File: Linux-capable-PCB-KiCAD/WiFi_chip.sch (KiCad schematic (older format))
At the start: 2 parts

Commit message: Added some documents
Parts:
- added C? (x4): 100n, symbol device:C
- added C?: 5.6p, symbol device:C
- added L?: NC, symbol device:L
- added Y?: 26 MHz, symbol device:Crystal_GND23
- R?: symbol Device:R -> Linux-capable-PCB-KiCAD-rescue:R-Device
- U?: symbol ESP8089:ESP8089 -> Linux-capable-PCB-KiCAD-rescue:ESP8089-ESP8089
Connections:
- net labels added: SD_CLK, SD_CMD, SD_D0, SD_D1, SD_D2, SD_D3, VDD33, VDIO, WIFI_ANT, WIFI_EN
- wire segments 7 -> 59

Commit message: RAM cip je spojen
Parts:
- C? (x5): symbol device:C -> Linux-capable-PCB-KiCAD-rescue:C-device
- L?: symbol device:L -> Linux-capable-PCB-KiCAD-rescue:L-device
- Y?: symbol device:Crystal_GND23 -> Linux-capable-PCB-KiCAD-rescue:Crystal_GND23-device
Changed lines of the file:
@@
 $Descr A4 11693 8268
 encoding utf-8
-Sheet 3 3
+Sheet 3 4
 Title ""
 Date ""
@@
 Connection ~ 6600 4200
 $Comp
-L device:C C?
+L Linux-capable-PCB-KiCAD-rescue:C-device C?
 U 1 1 62B23B89
 P 6900 4450
@@
 	4550 3600 3300 3600
 $Comp
-L device:C C?
+L Linux-capable-PCB-KiCAD-rescue:C-device C?
 U 1 1 62B24ACF
 P 3000 3600
@@
 $EndComp
 $Comp
-L device:L L?
+L Linux-capable-PCB-KiCAD-rescue:L-device L?
 U 1 1 62B2523E
 P 3300 3900
@@
 Connection ~ 5350 1900
 $Comp
-L device:C C?
+L Linux-capable-PCB-KiCAD-rescue:C-device C?
 U 1 1 62B27ADB
 P 3800 2150
@@
 Connection ~ 3800 1900
 $Comp
-L device:Crystal_GND23 Y?
+L Linux-capable-PCB-KiCAD-rescue:Crystal_GND23-device Y?
 U 1 1 62B29AE8
 P 6050 1900
@@
 	6050 2100 6050 2150
 $Comp
-L device:C C?
+L Linux-capable-PCB-KiCAD-rescue:C-device C?
 U 1 1 62B2DA78
 P 5550 1450
@@
 $EndComp
 $Comp
-L device:C C?
+L Linux-capable-PCB-KiCAD-rescue:C-device C?
 U 1 1 62B2DE8D
 P 6800 1450

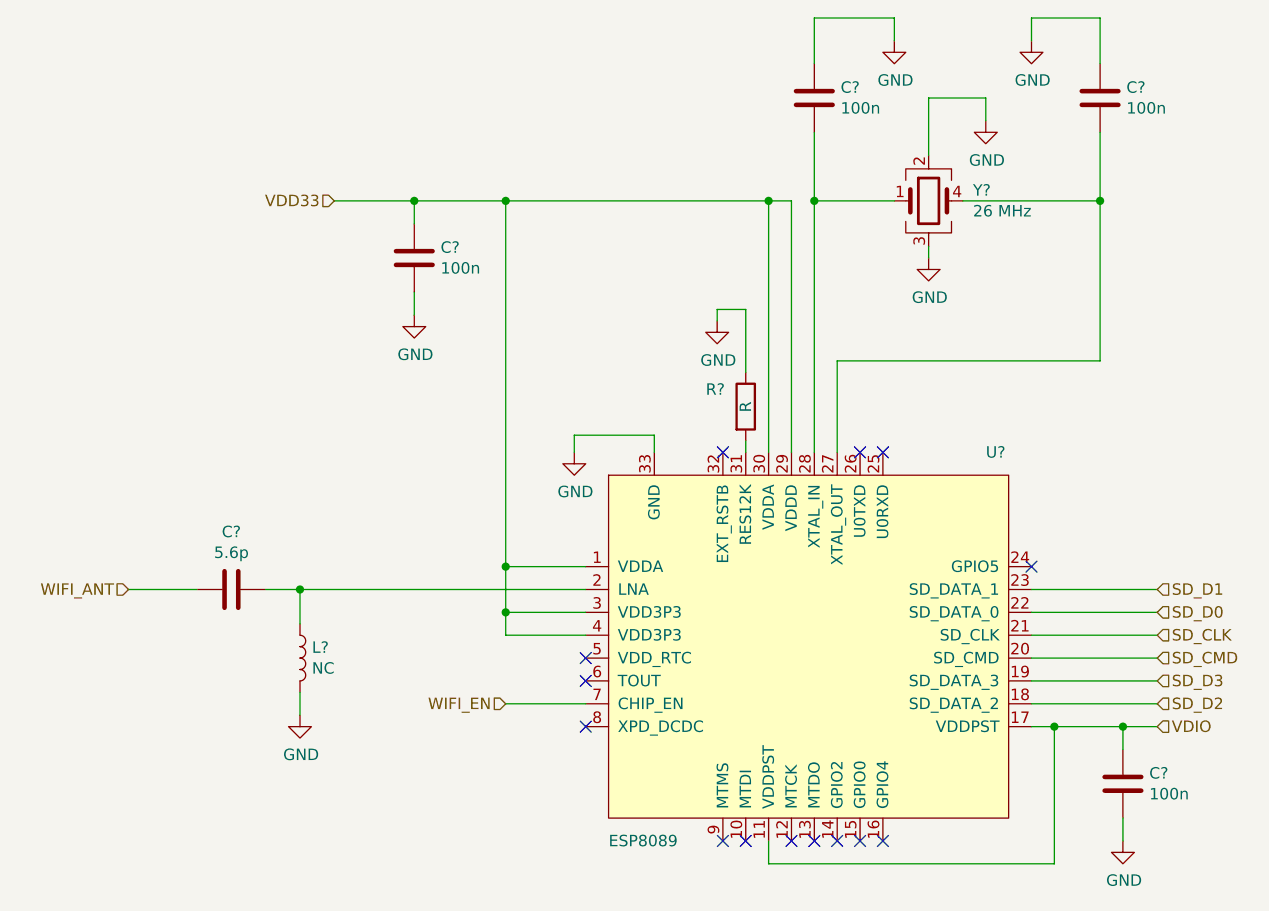
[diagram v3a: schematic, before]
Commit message: Power supply schematics
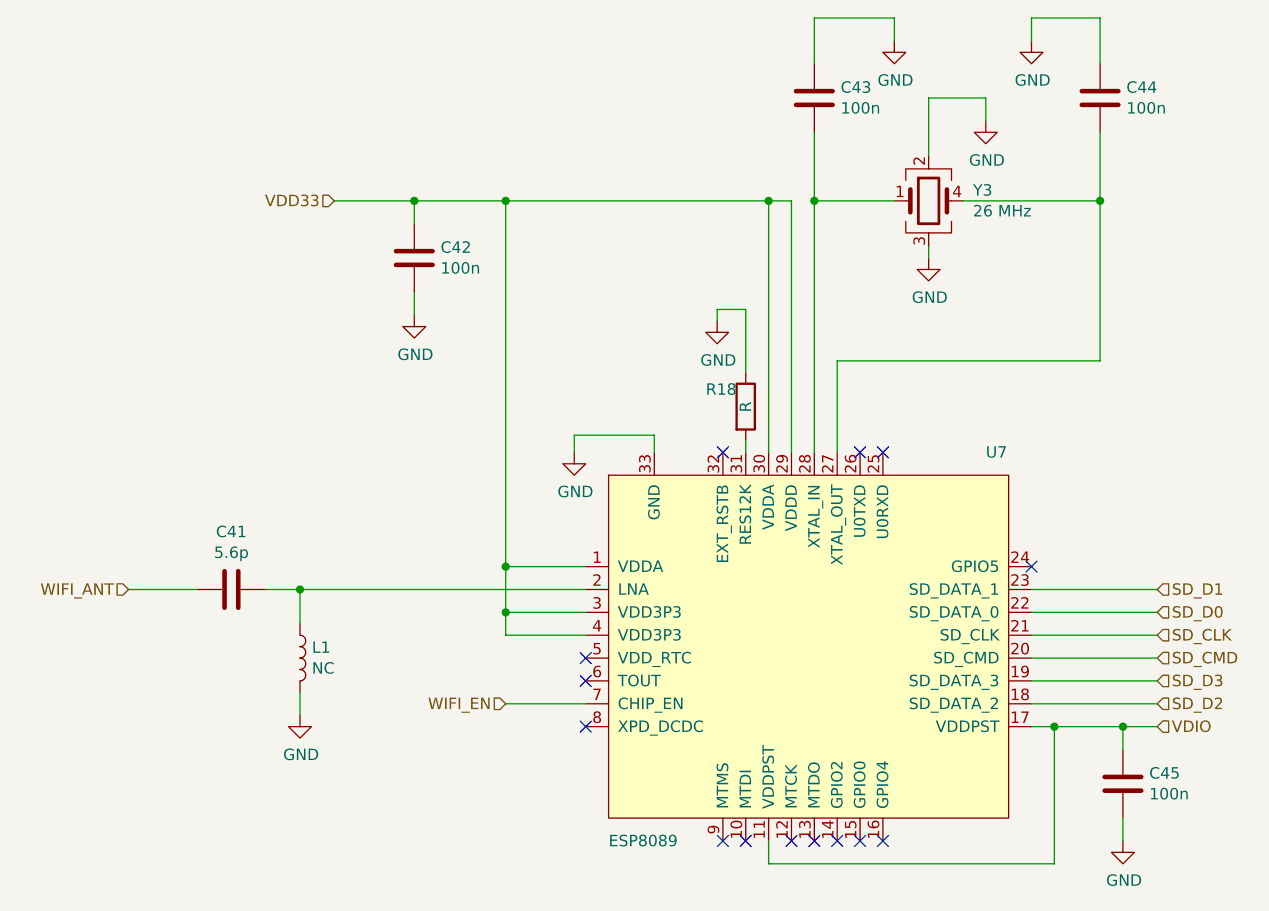
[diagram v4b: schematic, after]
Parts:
- gave numbers to parts that had none: 9
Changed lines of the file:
@@
 $EndDescr
 $Comp
-L Linux-capable-PCB-KiCAD-rescue:ESP8089-ESP8089 U?
+L Linux-capable-PCB-KiCAD-rescue:ESP8089-ESP8089 U7
 U 1 1 62B70BC0
 P 5650 3850
-F 0 "U?" H 6300 4700 50  0000 L CNN
+F 0 "U7" H 6300 4700 50  0000 L CNN
 F 1 "ESP8089" H 4650 3000 50  0000 L CNN
 F 2 "" H 5650 3850 50  0001 C CNN
@@
 NoConn ~ 4550 4000
 $Comp
-L power:GND #PWR?
+L power:GND #PWR0180
 U 1 1 62B757FB
 P 4500 3000
-F 0 "#PWR?" H 4500 2750 50  0001 C CNN
+F 0 "#PWR0180" H 4500 2750 50  0001 C CNN
 F 1 "GND" H 4505 2827 50  0000 C CNN
 F 2 "" H 4500 3000 50  0001 C CNN
@@
 P 5250 2800
 AR Path="/62B75FB1" Ref="R?"  Part="1"
-AR Path="/62FC6136/62B6FA43/62B75FB1" Ref="R?"  Part="1"
-F 0 "R?" H 5075 2875 50  0000 L CNN
+AR Path="/62FC6136/62B6FA43/62B75FB1" Ref="R18"  Part="1"
+F 0 "R18" H 5075 2875 50  0000 L CNN
 F 1 "R" V 5250 2775 50  0000 L CNN
 F 2 "" V 5180 2800 50  0001 C CNN
@@
 	5125 2425 5125 2375
 $Comp
-L power:GND #PWR?
+L power:GND #PWR0181
 U 1 1 62B76B5A
 P 5125 2425
-F 0 "#PWR?" H 5125 2175 50  0001 C CNN
+F 0 "#PWR0181" H 5125 2175 50  0001 C CNN
 F 1 "GND" H 5130 2252 50  0000 C CNN
 F 2 "" H 5125 2425 50  0001 C CNN
@@
 Connection ~ 6600 4200
 $Comp
-L Linux-capable-PCB-KiCAD-rescue:C-device C?
+L Linux-capable-PCB-KiCAD-rescue:C-device C45
 U 1 1 62B23B89
 P 6900 4450
-F 0 "C?" H 7015 4496 50  0000 L CNN
+F 0 "C45" H 7015 4496 50  0000 L CNN
 F 1 "100n" H 7015 4405 50  0000 L CNN
 F 2 "" H 6938 4300 50  0001 C CNN
@@
 $EndComp
 $Comp
-L power:GND #PWR?
+L power:GND #PWR0182
 U 1 1 62B24147
 P 6900 4700
-F 0 "#PWR?" H 6900 4450 50  0001 C CNN
+F 0 "#PWR0182" H 6900 4450 50  0001 C CNN
 F 1 "GND" H 6905 4527 50  0000 C CNN
 F 2 "" H 6900 4700 50  0001 C CNN
@@
 	4550 3600 3300 3600
 $Comp
-L Linux-capable-PCB-KiCAD-rescue:C-device C?
+L Linux-capable-PCB-KiCAD-rescue:C-device C41
 U 1 1 62B24ACF
 P 3000 3600
-F 0 "C?" V 2748 3600 50  0000 C CNN
+F 0 "C41" V 2748 3600 50  0000 C CNN
 F 1 "5.6p" V 2839 3600 50  0000 C CNN
 F 2 "" H 3038 3450 50  0001 C CNN
@@
 $EndComp
 $Comp
-L Linux-capable-PCB-KiCAD-rescue:L-device L?
+L Linux-capable-PCB-KiCAD-rescue:L-device L1
 U 1 1 62B2523E
 P 3300 3900
-F 0 "L?" H 3352 3946 50  0000 L CNN
+F 0 "L1" H 3352 3946 50  0000 L CNN
 F 1 "NC" H 3352 3855 50  0000 L CNN
 F 2 "" H 3300 3900 50  0001 C CNN
@@
 	3300 3600 3150 3600
 $Comp
-L power:GND #PWR?
+L power:GND #PWR0183
 U 1 1 62B25A7D
 P 3300 4150
-F 0 "#PWR?" H 3300 3900 50  0001 C CNN
+F 0 "#PWR0183" H 3300 3900 50  0001 C CNN
 F 1 "GND" H 3305 3977 50  0000 C CNN
 F 2 "" H 3300 4150 50  0001 C CNN
@@
 Connection ~ 5350 1900
 $Comp
-L Linux-capable-PCB-KiCAD-rescue:C-device C?
+L Linux-capable-PCB-KiCAD-rescue:C-device C42
 U 1 1 62B27ADB
 P 3800 2150
-F 0 "C?" H 3915 2196 50  0000 L CNN
+F 0 "C42" H 3915 2196 50  0000 L CNN
 F 1 "100n" H 3915 2105 50  0000 L CNN
 F 2 "" H 3838 2000 50  0001 C CNN
@@
 $EndComp
 $Comp
-L power:GND #PWR?
+L power:GND #PWR0184
 U 1 1 62B28059
 P 3800 2400
-F 0 "#PWR?" H 3800 2150 50  0001 C CNN
+F 0 "#PWR0184" H 3800 2150 50  0001 C CNN
 F 1 "GND" H 3805 2227 50  0000 C CNN
 F 2 "" H 3800 2400 50  0001 C CNN
@@
 Connection ~ 3800 1900
 $Comp
-L Linux-capable-PCB-KiCAD-rescue:Crystal_GND23-device Y?
+L Linux-capable-PCB-KiCAD-rescue:Crystal_GND23-device Y3
 U 1 1 62B29AE8
 P 6050 1900
-F 0 "Y?" H 6244 1946 50  0000 L CNN
+F 0 "Y3" H 6244 1946 50  0000 L CNN
 F 1 "26 MHz" H 6244 1855 50  0000 L CNN
 F 2 "" H 6050 1900 50  0001 C CNN
@@
 	6800 1900 6200 1900
 $Comp
-L power:GND #PWR?
+L power:GND #PWR0185
 U 1 1 62B2C07E
 P 6050 2150
-F 0 "#PWR?" H 6050 1900 50  0001 C CNN
+F 0 "#PWR0185" H 6050 1900 50  0001 C CNN
 F 1 "GND" H 6055 1977 50  0000 C CNN
 F 2 "" H 6050 2150 50  0001 C CNN
@@
 $EndComp
 $Comp
-L power:GND #PWR?
+L power:GND #PWR0186
 U 1 1 62B2C41E
 P 6300 1550
-F 0 "#PWR?" H 6300 1300 50  0001 C CNN
+F 0 "#PWR0186" H 6300 1300 50  0001 C CNN
 F 1 "GND" H 6305 1377 50  0000 C CNN
 F 2 "" H 6300 1550 50  0001 C CNN
@@
 	6050 2100 6050 2150
 $Comp
-L Linux-capable-PCB-KiCAD-rescue:C-device C?
+L Linux-capable-PCB-KiCAD-rescue:C-device C43
 U 1 1 62B2DA78
 P 5550 1450
-F 0 "C?" H 5665 1496 50  0000 L CNN
+F 0 "C43" H 5665 1496 50  0000 L CNN
 F 1 "100n" H 5665 1405 50  0000 L CNN
 F 2 "" H 5588 1300 50  0001 C CNN
@@
 $EndComp
 $Comp
-L Linux-capable-PCB-KiCAD-rescue:C-device C?
+L Linux-capable-PCB-KiCAD-rescue:C-device C44
 U 1 1 62B2DE8D
 P 6800 1450
-F 0 "C?" H 6915 1496 50  0000 L CNN
+F 0 "C44" H 6915 1496 50  0000 L CNN
 F 1 "100n" H 6915 1405 50  0000 L CNN
 F 2 "" H 6838 1300 50  0001 C CNN
@@
 Connection ~ 6800 1900
 $Comp
-L power:GND #PWR?
+L power:GND #PWR0187
 U 1 1 62B2F68F
 P 5900 1200
-F 0 "#PWR?" H 5900 950 50  0001 C CNN
+F 0 "#PWR0187" H 5900 950 50  0001 C CNN
 F 1 "GND" H 5905 1027 50  0000 C CNN
 F 2 "" H 5900 1200 50  0001 C CNN
@@
 $EndComp
 $Comp
-L power:GND #PWR?
+L power:GND #PWR0188
 U 1 1 62B2F9B3
 P 6500 1200
-F 0 "#PWR?" H 6500 950 50  0001 C CNN
+F 0 "#PWR0188" H 6500 950 50  0001 C CNN
 F 1 "GND" H 6505 1027 50  0000 C CNN
 F 2 "" H 6500 1200 50  0001 C CNN

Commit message: Assigned footprints to components, antenna and a couple of other footprints need to be assigned
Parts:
- C41, C42, C43, C44, C45: footprint (none) -> Capacitor_SMD:C_0603_1608Metric
- L1: footprint (none) -> Inductor_SMD:L_0603_1608Metric
- R18: footprint (none) -> Resistor_SMD:R_0603_1608Metric
- U7: footprint (none) -> Package_DFN_QFN:QFN-32-1EP_5x5mm_P0.5mm_EP3.7x3.7mm
- Y3: footprint (none) -> Crystal:Crystal_SMD_EuroQuartz_MJ-4Pin_5.0x3.2mm
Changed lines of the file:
@@
 F 0 "U7" H 6300 4700 50  0000 L CNN
 F 1 "ESP8089" H 4650 3000 50  0000 L CNN
-F 2 "" H 5650 3850 50  0001 C CNN
+F 2 "Package_DFN_QFN:QFN-32-1EP_5x5mm_P0.5mm_EP3.7x3.7mm" H 5650 3850 50  0001 C CNN
 F 3 "" H 5650 3850 50  0001 C CNN
 	1    5650 3850
@@
 F 0 "R18" H 5075 2875 50  0000 L CNN
 F 1 "R" V 5250 2775 50  0000 L CNN
-F 2 "" V 5180 2800 50  0001 C CNN
+F 2 "Resistor_SMD:R_0603_1608Metric" V 5180 2800 50  0001 C CNN
 F 3 "~" H 5250 2800 50  0001 C CNN
 	1    5250 2800
@@
 F 0 "C45" H 7015 4496 50  0000 L CNN
 F 1 "100n" H 7015 4405 50  0000 L CNN
-F 2 "" H 6938 4300 50  0001 C CNN
+F 2 "Capacitor_SMD:C_0603_1608Metric" H 6938 4300 50  0001 C CNN
 F 3 "" H 6900 4450 50  0001 C CNN
 	1    6900 4450
@@
 F 0 "C41" V 2748 3600 50  0000 C CNN
 F 1 "5.6p" V 2839 3600 50  0000 C CNN
-F 2 "" H 3038 3450 50  0001 C CNN
+F 2 "Capacitor_SMD:C_0603_1608Metric" H 3038 3450 50  0001 C CNN
 F 3 "" H 3000 3600 50  0001 C CNN
 	1    3000 3600
@@
 F 0 "L1" H 3352 3946 50  0000 L CNN
 F 1 "NC" H 3352 3855 50  0000 L CNN
-F 2 "" H 3300 3900 50  0001 C CNN
+F 2 "Inductor_SMD:L_0603_1608Metric" H 3300 3900 50  0001 C CNN
 F 3 "" H 3300 3900 50  0001 C CNN
 	1    3300 3900
@@
 F 0 "C42" H 3915 2196 50  0000 L CNN
 F 1 "100n" H 3915 2105 50  0000 L CNN
-F 2 "" H 3838 2000 50  0001 C CNN
+F 2 "Capacitor_SMD:C_0603_1608Metric" H 3838 2000 50  0001 C CNN
 F 3 "" H 3800 2150 50  0001 C CNN
 	1    3800 2150
@@
 F 0 "Y3" H 6244 1946 50  0000 L CNN
 F 1 "26 MHz" H 6244 1855 50  0000 L CNN
-F 2 "" H 6050 1900 50  0001 C CNN
+F 2 "Crystal:Crystal_SMD_EuroQuartz_MJ-4Pin_5.0x3.2mm" H 6050 1900 50  0001 C CNN
 F 3 "" H 6050 1900 50  0001 C CNN
 	1    6050 1900
@@
 F 0 "C43" H 5665 1496 50  0000 L CNN
 F 1 "100n" H 5665 1405 50  0000 L CNN
-F 2 "" H 5588 1300 50  0001 C CNN
+F 2 "Capacitor_SMD:C_0603_1608Metric" H 5588 1300 50  0001 C CNN
 F 3 "" H 5550 1450 50  0001 C CNN
 	1    5550 1450
@@
 F 0 "C44" H 6915 1496 50  0000 L CNN
 F 1 "100n" H 6915 1405 50  0000 L CNN
-F 2 "" H 6838 1300 50  0001 C CNN
+F 2 "Capacitor_SMD:C_0603_1608Metric" H 6838 1300 50  0001 C CNN
 F 3 "" H 6800 1450 50  0001 C CNN
 	1    6800 1450
